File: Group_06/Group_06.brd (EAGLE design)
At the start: 72.4 x 63.5 mm, 29 parts, among them J1 POWER_JACKPTH_LOCK, U2 +12v

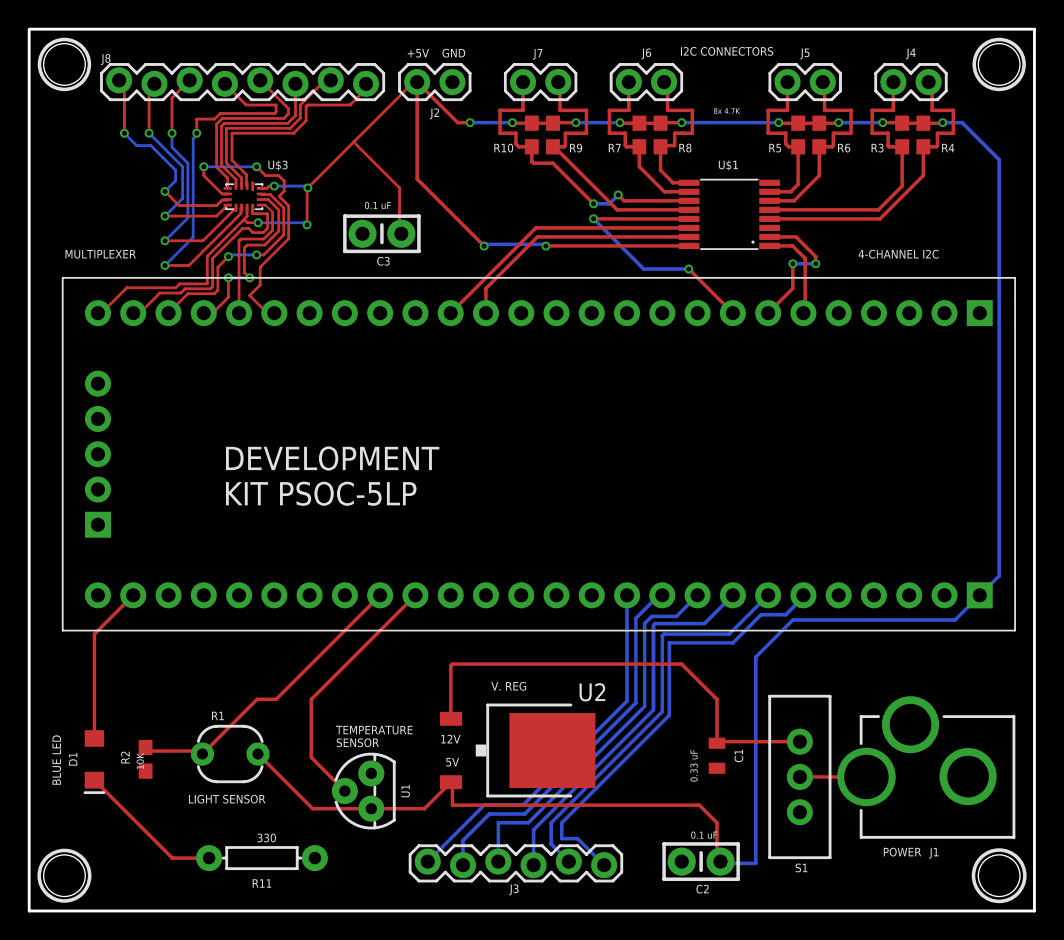
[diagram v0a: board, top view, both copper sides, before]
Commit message: Adding component silkscreen
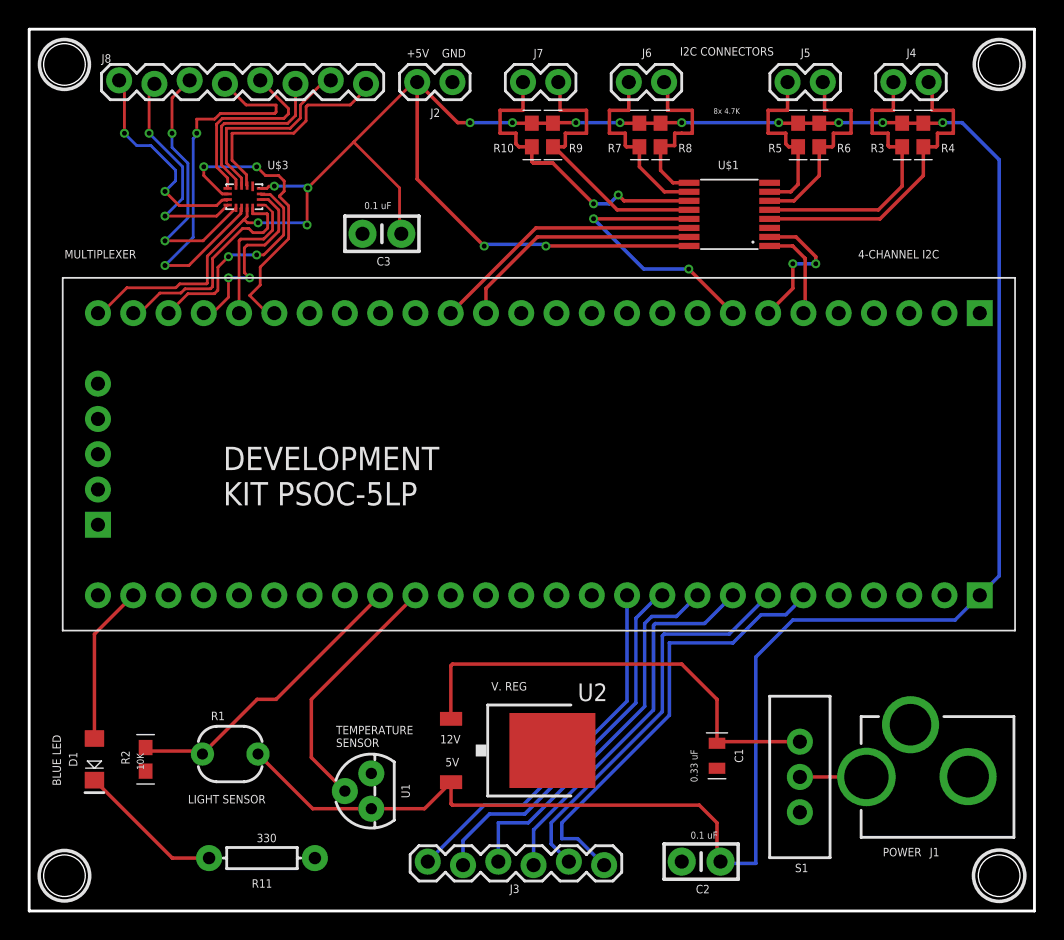
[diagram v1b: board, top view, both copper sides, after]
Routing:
- net I2C_SDA_3: track 22.6 -> 23.9 mm
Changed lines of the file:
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@@
 <drawing>
 <settings>
-<setting alwaysvectorfont="no"/>
+<setting alwaysvectorfont="yes"/>
 <setting verticaltext="up"/>
 </settings>
@@
 <layer number="26" name="bNames" color="7" fill="1" visible="yes" active="yes"/>
 <layer number="27" name="tValues" color="7" fill="1" visible="no" active="yes"/>
-<layer number="28" name="bValues" color="7" fill="1" visible="no" active="yes"/>
-<layer number="29" name="tStop" color="7" fill="3" visible="yes" active="yes"/>
+<layer number="28" name="bValues" color="7" fill="1" visible="yes" active="yes"/>
+<layer number="29" name="tStop" color="7" fill="3" visible="no" active="yes"/>
 <layer number="30" name="bStop" color="7" fill="6" visible="no" active="yes"/>
 <layer number="31" name="tCream" color="7" fill="4" visible="no" active="yes"/>
@@
 <layer number="37" name="tTest" color="7" fill="1" visible="no" active="yes"/>
 <layer number="38" name="bTest" color="7" fill="1" visible="no" active="yes"/>
-<layer number="39" name="tKeepout" color="4" fill="11" visible="yes" active="yes"/>
-<layer number="40" name="bKeepout" color="1" fill="11" visible="yes" active="yes"/>
-<layer number="41" name="tRestrict" color="4" fill="10" visible="yes" active="yes"/>
-<layer number="42" name="bRestrict" color="1" fill="10" visible="yes" active="yes"/>
+<layer number="39" name="tKeepout" color="4" fill="11" visible="no" active="yes"/>
+<layer number="40" name="bKeepout" color="1" fill="11" visible="no" active="yes"/>
+<layer number="41" name="tRestrict" color="4" fill="10" visible="no" active="yes"/>
+<layer number="42" name="bRestrict" color="1" fill="10" visible="no" active="yes"/>
 <layer number="43" name="vRestrict" color="2" fill="10" visible="no" active="yes"/>
 <layer number="44" name="Drills" color="7" fill="1" visible="no" active="yes"/>
-<layer number="45" name="Holes" color="7" fill="1" visible="no" active="yes"/>
+<layer number="45" name="Holes" color="7" fill="1" visible="yes" active="yes"/>
 <layer number="46" name="Milling" color="3" fill="1" visible="no" active="yes"/>
 <layer number="47" name="Measures" color="7" fill="1" visible="no" active="yes"/>
@@
 <circle x="2.54" y="60.96" radius="1.79605" width="0.254" layer="21"/>
 <circle x="2.54" y="2.54" radius="1.8183625" width="0.254" layer="21"/>
+<wire x1="43.307" y1="57.658" x2="44.577" y2="57.658" width="0.1016" layer="21"/>
+<wire x1="46.101" y1="57.658" x2="44.831" y2="57.658" width="0.1016" layer="21"/>
+<wire x1="35.56" y1="57.658" x2="36.83" y2="57.658" width="0.1016" layer="21"/>
+<wire x1="38.354" y1="57.658" x2="37.084" y2="57.658" width="0.1016" layer="21"/>
+<wire x1="38.354" y1="54.102" x2="37.084" y2="54.102" width="0.1016" layer="21"/>
+<wire x1="35.56" y1="54.102" x2="36.83" y2="54.102" width="0.1016" layer="21"/>
+<wire x1="43.307" y1="54.102" x2="44.577" y2="54.102" width="0.1016" layer="21"/>
+<wire x1="44.831" y1="54.102" x2="46.101" y2="54.102" width="0.1016" layer="21"/>
+<wire x1="54.737" y1="57.658" x2="56.007" y2="57.658" width="0.1016" layer="21"/>
+<wire x1="56.261" y1="57.658" x2="57.531" y2="57.658" width="0.1016" layer="21"/>
+<wire x1="54.737" y1="54.102" x2="56.007" y2="54.102" width="0.1016" layer="21"/>
+<wire x1="56.261" y1="54.102" x2="57.531" y2="54.102" width="0.1016" layer="21"/>
+<wire x1="62.23" y1="57.658" x2="63.5" y2="57.658" width="0.1016" layer="21"/>
+<wire x1="63.754" y1="57.658" x2="65.024" y2="57.658" width="0.1016" layer="21"/>
+<wire x1="62.23" y1="54.102" x2="63.5" y2="54.102" width="0.1016" layer="21"/>
+<wire x1="63.754" y1="54.102" x2="65.024" y2="54.102" width="0.1016" layer="21"/>
+<wire x1="4.191" y1="10.795" x2="4.699" y2="10.287" width="0.1016" layer="21"/>
+<wire x1="4.699" y1="10.287" x2="5.207" y2="10.795" width="0.1016" layer="21"/>
+<wire x1="7.747" y1="12.7" x2="9.017" y2="12.7" width="0.1016" layer="21"/>
+<wire x1="7.747" y1="9.144" x2="9.017" y2="9.144" width="0.1016" layer="21"/>
+<wire x1="4.064" y1="10.287" x2="5.334" y2="10.287" width="0.1016" layer="21"/>
+<wire x1="48.768" y1="12.827" x2="50.292" y2="12.827" width="0.1016" layer="21"/>
+<wire x1="48.895" y1="9.525" x2="50.165" y2="9.525" width="0.1016" layer="21"/>
+<wire x1="4.191" y1="10.795" x2="5.207" y2="10.795" width="0.1016" layer="21"/>
 </plain>
 <attributes>
@@
 <vertex x="72.39" y="0"/>
 </polygon>
-<wire x1="24.638" y1="7.366" x2="24.13" y2="7.366" width="0.254" layer="1"/>
-<wire x1="24.13" y1="7.366" x2="20.415" y2="7.366" width="0.254" layer="1"/>
+<wire x1="24.638" y1="7.366" x2="20.415" y2="7.366" width="0.254" layer="1"/>
 <wire x1="20.415" y1="7.366" x2="16.478" y2="11.303" width="0.254" layer="1"/>
 <wire x1="47.519" y1="47.89" x2="37.222" y2="47.89" width="0.254" layer="1"/>
@@
 <wire x1="26.67" y1="48.895" x2="26.67" y2="52.07" width="0.2032" layer="1"/>
 <wire x1="26.67" y1="52.07" x2="23.368" y2="55.372" width="0.2032" layer="1"/>
-<wire x1="30.226" y1="9.124" x2="30.379" y2="9.277" width="0.254" layer="1"/>
 <wire x1="49.784" y1="3.556" x2="49.53" y2="3.81" width="0.254" layer="1"/>
 <wire x1="49.53" y1="3.81" x2="49.53" y2="6.35" width="0.254" layer="1"/>
 <wire x1="49.53" y1="6.35" x2="48.26" y2="7.62" width="0.254" layer="1"/>
 <wire x1="48.26" y1="7.62" x2="30.48" y2="7.62" width="0.254" layer="1"/>
-<wire x1="30.48" y1="7.62" x2="30.48" y2="8.89" width="0.254" layer="1"/>
+<wire x1="28.468" y1="7.366" x2="24.638" y2="7.366" width="0.254" layer="1"/>
+<wire x1="30.48" y1="7.62" x2="30.379" y2="7.721" width="0.254" layer="1"/>
+<wire x1="30.379" y1="7.721" x2="30.379" y2="9.277" width="0.254" layer="1"/>
 <wire x1="30.379" y1="9.277" x2="28.468" y2="7.366" width="0.254" layer="1"/>
-<wire x1="28.468" y1="7.366" x2="24.638" y2="7.366" width="0.254" layer="1"/>
 </signal>
 <signal name="PHOTO_OUT">
@@
 <contactref element="U2" pad="1"/>
 <contactref element="S1" pad="1"/>
-<wire x1="30.226" y1="13.99" x2="30.363" y2="13.853" width="0.254" layer="1"/>
 <wire x1="30.363" y1="13.853" x2="30.379" y2="13.837" width="0.254" layer="1"/>
 <wire x1="55.499" y1="12.192" x2="49.646" y2="12.192" width="0.254" layer="1"/>
@@
 <wire x1="49.53" y1="12.076" x2="49.53" y2="15.24" width="0.254" layer="1"/>
 <wire x1="46.99" y1="17.78" x2="30.48" y2="17.78" width="0.254" layer="1"/>
+<wire x1="49.53" y1="15.24" x2="46.99" y2="17.78" width="0.254" layer="1"/>
 <wire x1="30.48" y1="17.78" x2="30.363" y2="17.663" width="0.254" layer="1"/>
 <wire x1="30.363" y1="17.663" x2="30.363" y2="13.853" width="0.254" layer="1"/>
-<wire x1="49.53" y1="15.24" x2="46.99" y2="17.78" width="0.254" layer="1"/>
 </signal>
 <signal name="I2C_SCL_0">
@@
 <wire x1="33.909" y1="57.658" x2="35.56" y2="57.658" width="0.254" layer="1"/>
 <wire x1="35.56" y1="57.658" x2="35.56" y2="59.69" width="0.254" layer="1"/>
+<wire x1="36.322" y1="53.848" x2="37.719" y2="53.848" width="0.254" layer="1"/>
 </signal>
 <signal name="I2C_SDA">
@@
 <via x="9.779" y="48.26" extent="1-16" drill="0.35"/>
 <wire x1="9.779" y1="48.26" x2="12.5174" y2="48.26" width="0.2032" layer="1"/>
-<wire x1="12.5174" y1="48.26" x2="14.8924" y2="50.635" width="0.2032" layer="1"/>
-<wire x1="14.8924" y1="50.635" x2="14.894" y2="50.635" width="0" layer="19" extent="1-1"/>
+<wire x1="14.894" y1="50.635" x2="12.519" y2="48.26" width="0.2032" layer="1"/>
+<wire x1="12.519" y1="48.26" x2="12.5174" y2="48.26" width="0.2032" layer="1"/>
 </signal>
 <signal name="N$15">

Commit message: shrinking the board
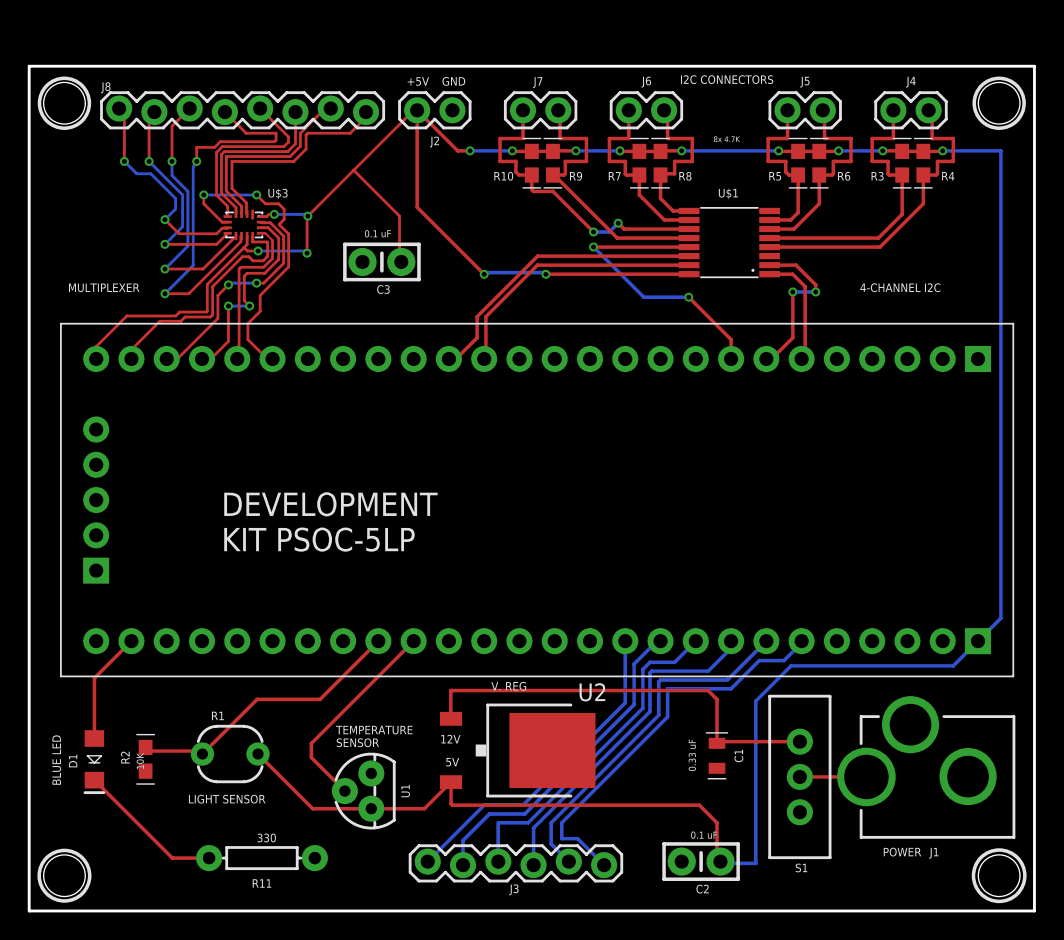
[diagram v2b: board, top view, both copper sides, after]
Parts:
- moved U$2 3.30 mm to (37.8, 30.9)
- moved C3 2.03 mm to (25.4, 46.7)
- moved R10 2.03 mm to (36.2, 53.8)
- moved R3 2.03 mm to (62.9, 53.8)
- moved R4 2.03 mm to (64.4, 53.8)
- moved R5 2.03 mm to (55.4, 53.8)
- moved R6 2.03 mm to (56.9, 53.8)
- moved R7 2.03 mm to (43.9, 53.8)
- moved R8 2.03 mm to (45.5, 53.8)
- moved R9 2.03 mm to (37.7, 53.8)
- moved U$3 2.03 mm to (15.5, 49.4)
- moved J2 2.03 mm to (30.5, 57.7)
- moved J4 2.03 mm to (64.8, 57.7)
- moved J5 2.03 mm to (57.1, 57.7)
- moved J6 2.03 mm to (45.7, 57.7)
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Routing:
- net N$6: track 27.0 -> 23.7 mm
- net N$18: track 32.3 -> 28.9 mm
- net N$7: track 27.4 -> 24.1 mm
- net N$3: track 11.5 -> 8.11 mm
- net TEMP_OUT: track 18.2 -> 14.8 mm
- net N$5: track 26.8 -> 23.4 mm
- net N$9: track 28.9 -> 25.6 mm
- net N$8: track 27.5 -> 24.4 mm
- net 12V: track 33.3 -> 30.7 mm
- net I2C_A1: track 10.4 -> 11.9 mm
- net I2C_SCL: track 19.7 -> 21.3 mm
- net PHOTO_OUT: track 21.8 -> 20.3 mm
- net I2C_SDA_3: track 23.9 -> 22.6 mm
- net I2C_SDA: track 17.9 -> 19.3 mm
- net MUX_A1: track 13.6 -> 14.9 mm
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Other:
- board size 72.4 x 63.5 mm -> 72.4 x 60.8 mm
